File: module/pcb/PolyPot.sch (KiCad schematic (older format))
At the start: 34 parts, among them J1 V_BAT_1S, J2 PROG/DEBUG, J3 ANALOG_CONN, J4 TOF_DIST_SENS, J5 M3, J6 M3, J7 M3, J8 M3, M1 DC_WATER_PUMP, Q1 Q_NMOS_DGS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

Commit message: Update pin assignment, add user button, add luminosity conn
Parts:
- added J9: LUMINOSITY_CONN, Socket_Strips:Socket_Strip_Straight_1x03_Pitch2.00mm, symbol Conn_01x03
- added R7, R9: 10k, Resistors_SMD:R_0603_HandSoldering, symbol R
- added R8: 470, Resistors_SMD:R_0603_HandSoldering, symbol R
- added SW3: USR_BTN, Socket_Strips:Socket_Strip_Straight_1x02_Pitch2.00mm, symbol SW_Push
- added TP5: TEST, Socket_Strips:Socket_Strip_Straight_1x01_Pitch1.27mm, symbol TEST
- J3: value ANALOG_CONN -> HUMIDITY_CONN
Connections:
- net labels added: SENS_LUMINOSITY, USER_BTN, USER_BUTTON
- wire segments 56 -> 73
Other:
- note added: "(ADC1_CH4)"
- note added: "(ADC1_CH5)"
- note added: "(ADC1_CH7)"
- note added: "TODO:\n- choose motor NMOS\n- update V_Reg to AP7365-33ERG-13"
- moved on the sheet: C1, C4, J2, R3, R4, SW1, SW2, TP3, TP4, U2, U3

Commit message: PCB: update voltage regulator
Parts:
- removed U1: MCP1703A-3002_SOT89, TO_SOT_Packages_SMD:SOT89-3_Housing, symbol MCP1703A-3002_SOT89
- added U1: AP7365-XXEG_SOT223, TO_SOT_Packages_SMD:SOT-223, symbol AP7365-XXEG_SOT223
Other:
- note added: "TODO:\n- choose motor NMOS"
- note removed: "TODO:\n- choose motor NMOS\n- update V_Reg to AP7365-33ERG-13"
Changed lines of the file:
@@
-$EndComp
-$Comp
-L MCP1703A-3002_SOT89 U1
-U 1 1 59FF39A2
-P 2300 1150
-F 0 "U1" H 2150 1275 50  0000 C CNN
-F 1 "MCP1703A-3002_SOT89" H 1850 1400 50  0000 L CNN
-F 2 "TO_SOT_Packages_SMD:SOT89-3_Housing" H 2300 1350 50  0001 C CNN
-F 3 "" H 2300 1100 50  0001 C CNN
-	1    2300 1150
-	1    0    0    -1
 $EndComp
 $Comp
@@
 SENS_LUMINOSITY
 Text Notes 1050 7100 0    60   ~ 0
-TODO:\n- choose motor NMOS\n- update V_Reg to AP7365-33ERG-13
+TODO:\n- choose motor NMOS
+$Comp
+L AP7365-XXEG_SOT223 U1
+U 1 1 5A0DAEAA
+P 2300 1150
+F 0 "U1" H 2150 1450 60  0000 C CNN
+F 1 "AP7365-XXEG_SOT223" H 2300 1350 60  0000 C CNN
+F 2 "TO_SOT_Packages_SMD:SOT-223" H 2300 1150 60  0001 C CNN
+F 3 "" H 2300 1150 60  0001 C CNN
+	1    2300 1150
+	1    0    0    -1
+$EndComp
 $EndSCHEMATC

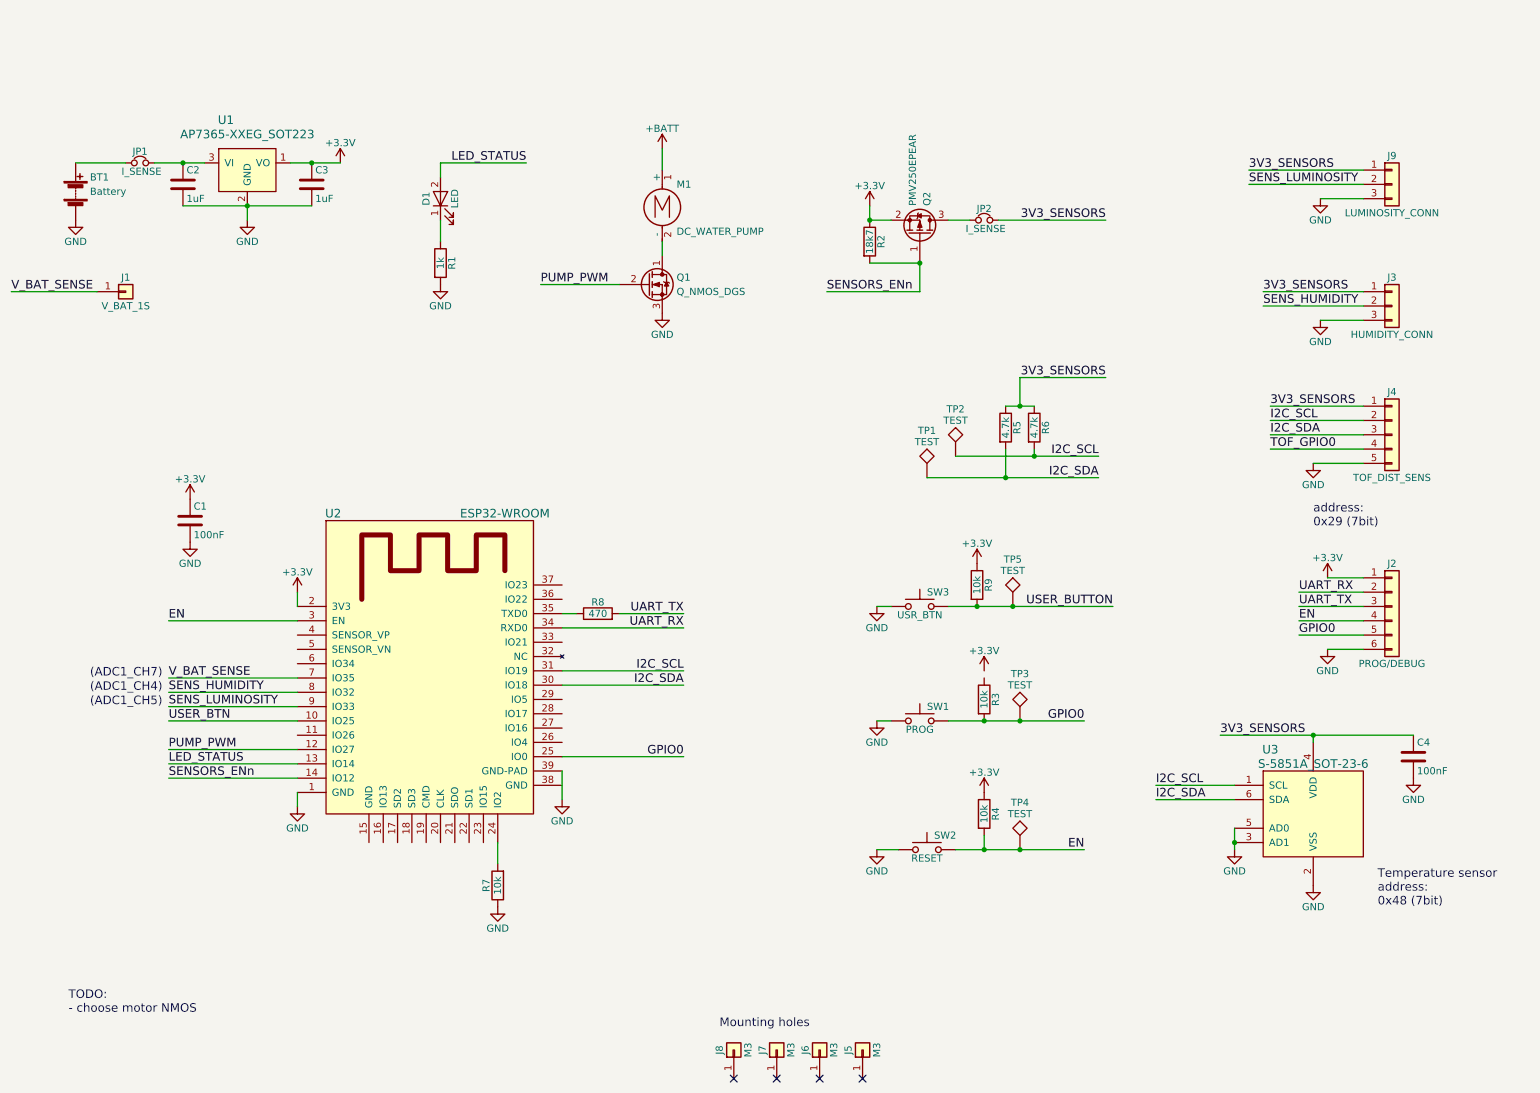
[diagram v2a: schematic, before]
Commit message: PCB: 3d model placement
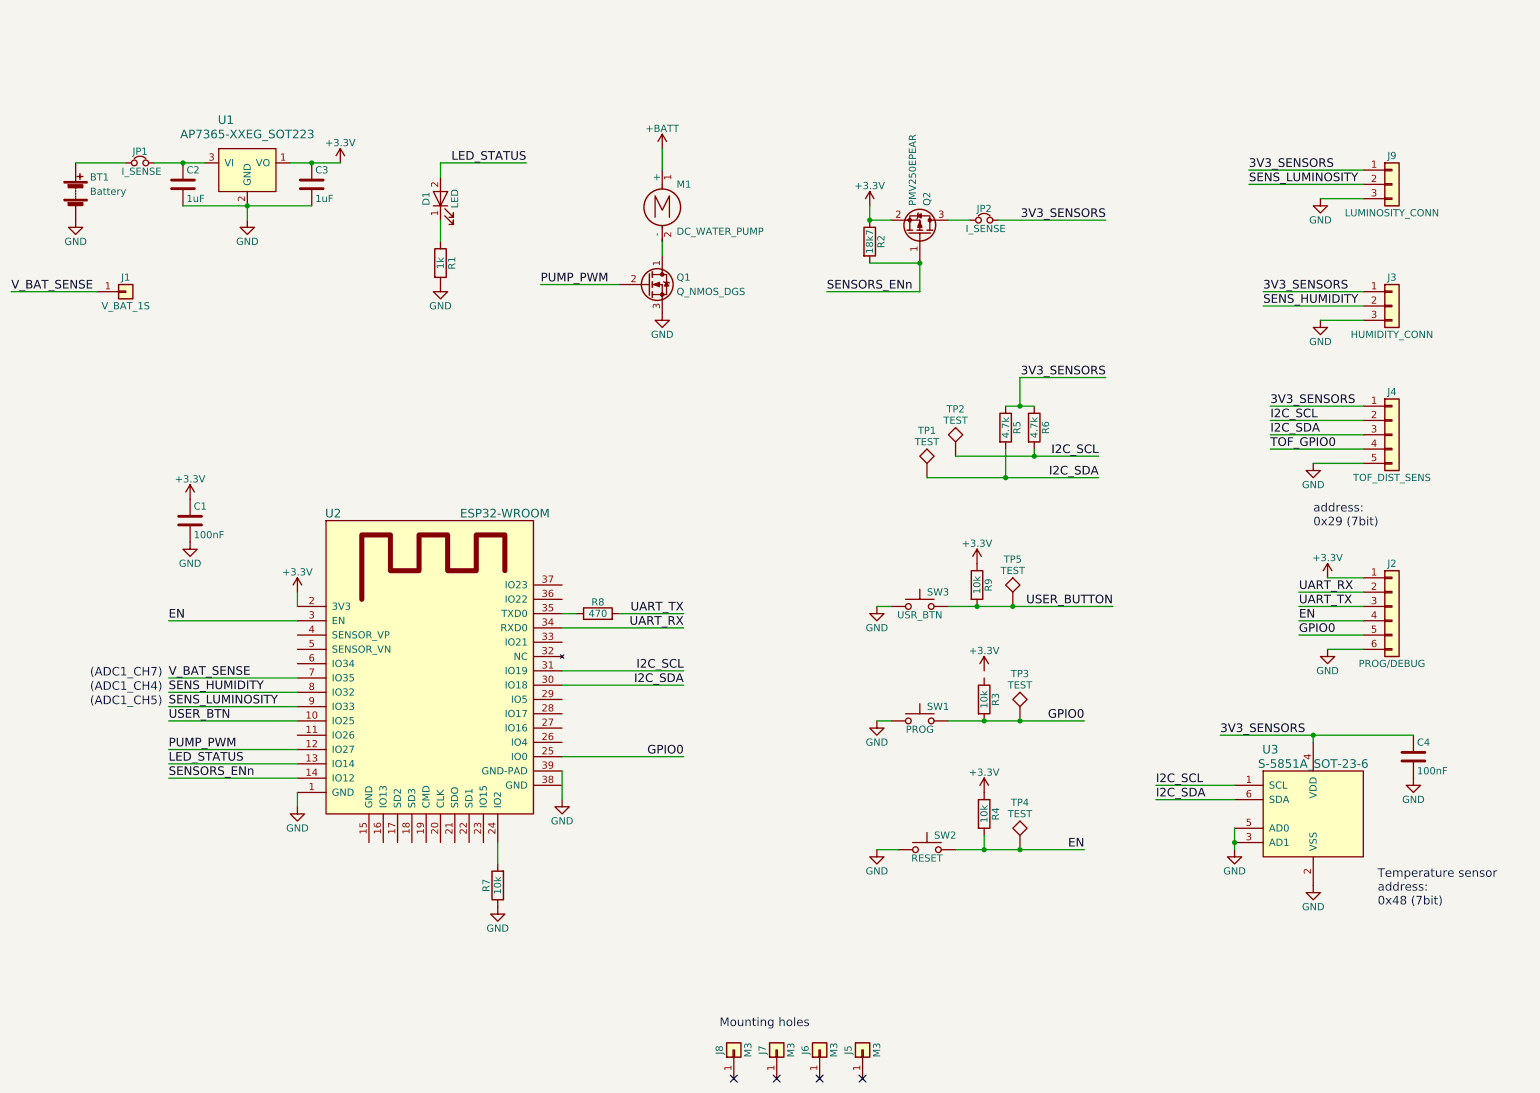
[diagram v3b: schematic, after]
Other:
- note removed: "TODO:\n- choose motor NMOS"
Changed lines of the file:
@@
 	1100 1150 1450 1150
 Wire Wire Line
-	1650 1150 2000 1150
+	1650 1150 1850 1150
+Wire Wire Line
+	1850 1150 2000 1150
 Connection ~ 1850 1150
 Connection ~ 2750 1150
 Connection ~ 2300 1450
 Wire Wire Line
-	1850 1450 2750 1450
+	1850 1450 2300 1450
+Wire Wire Line
+	2300 1450 2750 1450
 Wire Wire Line
 	2300 1550 2300 1450
 Wire Wire Line
-	2600 1150 2950 1150
+	2600 1150 2750 1150
+Wire Wire Line
+	2750 1150 2950 1150
 Wire Wire Line
 	2650 4150 2650 4250
@@
 	7450 5850 7450 5950
 Wire Wire Line
-	7250 5950 8150 5950
+	7250 5950 7450 5950
+Wire Wire Line
+	7450 5950 7700 5950
+Wire Wire Line
+	7700 5950 8150 5950
 Wire Wire Line
 	1750 4350 2650 4350
@@
 	9400 2150 10100 2150
 Wire Wire Line
-	7600 2850 7800 2850
+	7600 2850 7700 2850
+Wire Wire Line
+	7700 2850 7800 2850
 Wire Wire Line
 	7700 2850 7700 2650
@@
 	7600 3150 7600 3350
 Wire Wire Line
-	7050 3350 8250 3350
+	7050 3350 7600 3350
+Wire Wire Line
+	7600 3350 8250 3350
 Wire Wire Line
 	7800 3150 7800 3200
 Wire Wire Line
-	7250 3200 8250 3200
+	7250 3200 7800 3200
+Wire Wire Line
+	7800 3200 8250 3200
 Wire Wire Line
 	6650 1450 6650 1550
@@
 $EndComp
 Wire Wire Line
-	7200 5050 8150 5050
+	7200 5050 7450 5050
+Wire Wire Line
+	7450 5050 7700 5050
+Wire Wire Line
+	7700 5050 8150 5050
 $Comp
 L GND #PWR017
@@
 3V3_SENSORS
 Wire Wire Line
-	9100 5150 10450 5150
+	9100 5150 9750 5150
+Wire Wire Line
+	9750 5150 10450 5150
 Wire Wire Line
 	9750 5150 9750 5200
@@
 $EndComp
 Wire Wire Line
-	9200 5800 9200 5950
+	9200 5800 9200 5900
+Wire Wire Line
+	9200 5900 9200 5950
 Connection ~ 9200 5900
 Text Notes 10200 6350 0    60   ~ 0
@@
 	6700 4250 6800 4250
 Wire Wire Line
-	7200 4250 8350 4250
+	7200 4250 7400 4250
+Wire Wire Line
+	7400 4250 7650 4250
+Wire Wire Line
+	7650 4250 8350 4250
 $Comp
 L R R9
@@
 Text Label 1750 4950 0    60   ~ 0
 SENS_LUMINOSITY
-Text Notes 1050 7100 0    60   ~ 0
-TODO:\n- choose motor NMOS
 $Comp
 L AP7365-XXEG_SOT223 U1

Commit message: First PCB routage+ small correction int the schematics
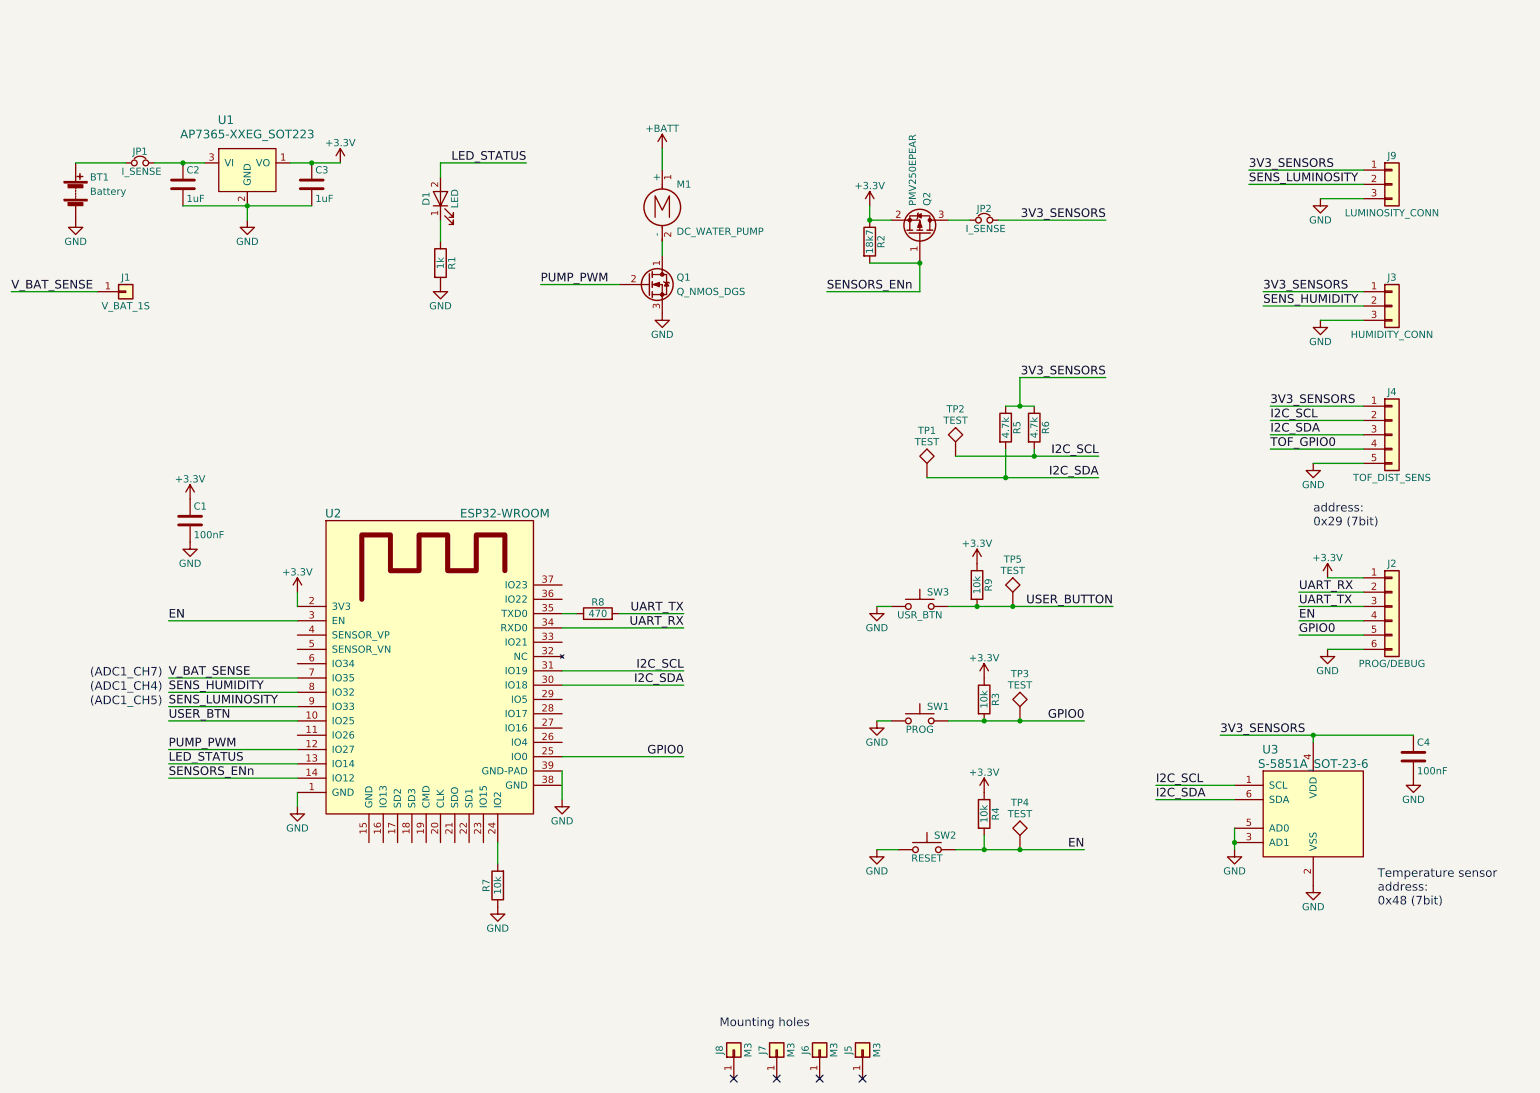
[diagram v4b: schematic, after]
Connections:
- net +3V3: now also R3.1
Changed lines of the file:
@@
 	1100 1150 1450 1150
 Wire Wire Line
-	1650 1150 1850 1150
-Wire Wire Line
-	1850 1150 2000 1150
+	1650 1150 2000 1150
 Connection ~ 1850 1150
 Connection ~ 2750 1150
 Connection ~ 2300 1450
 Wire Wire Line
-	1850 1450 2300 1450
-Wire Wire Line
-	2300 1450 2750 1450
+	1850 1450 2750 1450
 Wire Wire Line
 	2300 1550 2300 1450
 Wire Wire Line
-	2600 1150 2750 1150
-Wire Wire Line
-	2750 1150 2950 1150
+	2600 1150 2950 1150
 Wire Wire Line
 	2650 4150 2650 4250
@@
 	7450 5850 7450 5950
 Wire Wire Line
-	7250 5950 7450 5950
-Wire Wire Line
-	7450 5950 7700 5950
-Wire Wire Line
-	7700 5950 8150 5950
+	7250 5950 8150 5950
 Wire Wire Line
 	1750 4350 2650 4350
@@
 	9400 2150 10100 2150
 Wire Wire Line
-	7600 2850 7700 2850
-Wire Wire Line
-	7700 2850 7800 2850
+	7600 2850 7800 2850
 Wire Wire Line
 	7700 2850 7700 2650
@@
 	7600 3150 7600 3350
 Wire Wire Line
-	7050 3350 7600 3350
-Wire Wire Line
-	7600 3350 8250 3350
+	7050 3350 8250 3350
 Wire Wire Line
 	7800 3150 7800 3200
 Wire Wire Line
-	7250 3200 7800 3200
-Wire Wire Line
-	7800 3200 8250 3200
+	7250 3200 8250 3200
 Wire Wire Line
 	6650 1450 6650 1550
@@
 L +3.3V #PWR016
 U 1 1 59FFF2F8
-P 7450 4700
-F 0 "#PWR016" H 7450 4550 50  0001 C CNN
-F 1 "+3.3V" H 7450 4840 50  0000 C CNN
-F 2 "" H 7450 4700 50  0001 C CNN
-F 3 "" H 7450 4700 50  0001 C CNN
-	1    7450 4700
-	1    0    0    -1
-$EndComp
-Wire Wire Line
-	7200 5050 7450 5050
-Wire Wire Line
-	7450 5050 7700 5050
-Wire Wire Line
-	7700 5050 8150 5050
+P 7450 4750
+F 0 "#PWR016" H 7450 4600 50  0001 C CNN
+F 1 "+3.3V" H 7450 4890 50  0000 C CNN
+F 2 "" H 7450 4750 50  0001 C CNN
+F 3 "" H 7450 4750 50  0001 C CNN
+	1    7450 4750
+	1    0    0    -1
+$EndComp
+Wire Wire Line
+	7200 5050 8150 5050
 $Comp
 L GND #PWR017
@@
 3V3_SENSORS
 Wire Wire Line
-	9100 5150 9750 5150
-Wire Wire Line
-	9750 5150 10450 5150
+	9100 5150 10450 5150
 Wire Wire Line
 	9750 5150 9750 5200
@@
 $EndComp
 Wire Wire Line
-	9200 5800 9200 5900
-Wire Wire Line
-	9200 5900 9200 5950
+	9200 5800 9200 5950
 Connection ~ 9200 5900
 Text Notes 10200 6350 0    60   ~ 0
@@
 	6700 4250 6800 4250
 Wire Wire Line
-	7200 4250 7400 4250
-Wire Wire Line
-	7400 4250 7650 4250
-Wire Wire Line
-	7650 4250 8350 4250
+	7200 4250 8350 4250
 $Comp
 L R R9

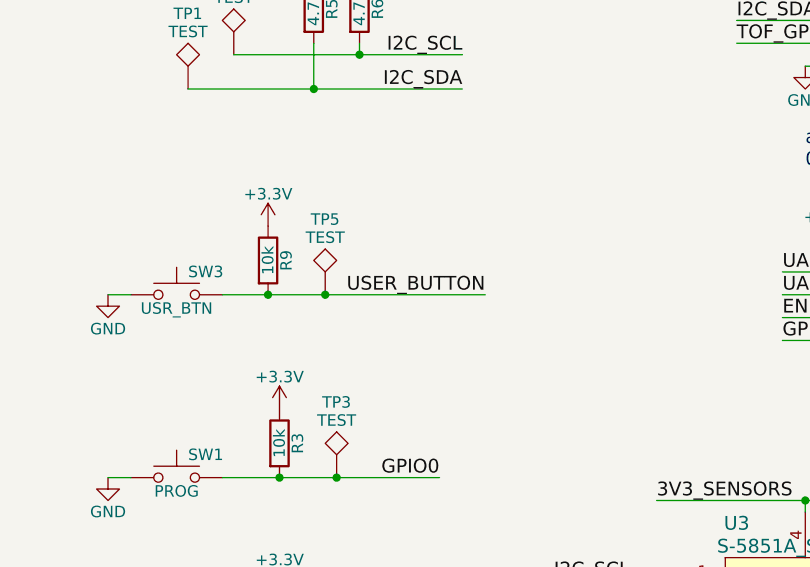
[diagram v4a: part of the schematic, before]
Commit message: Minor correction in the schematics
User_Button was improperly connected. There were two signals (user_button and user_btn) not linked to each other
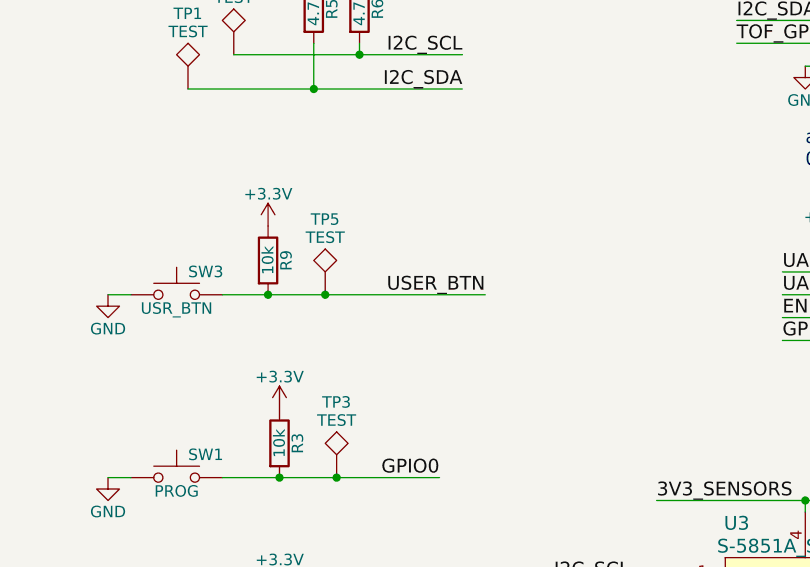
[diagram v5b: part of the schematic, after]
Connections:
- net USER_BUTTON is gone; now on net USER_BTN: R9.2, SW3.2, TP5.1
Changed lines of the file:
@@
 USER_BTN
 Text Label 8350 4250 2    60   ~ 0
-USER_BUTTON
+USER_BTN
 Wire Wire Line
 	1750 5050 2650 5050
